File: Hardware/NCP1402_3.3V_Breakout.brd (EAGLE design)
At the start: 12.7 x 16.5 mm, 12 parts, among them U1 NCP1402

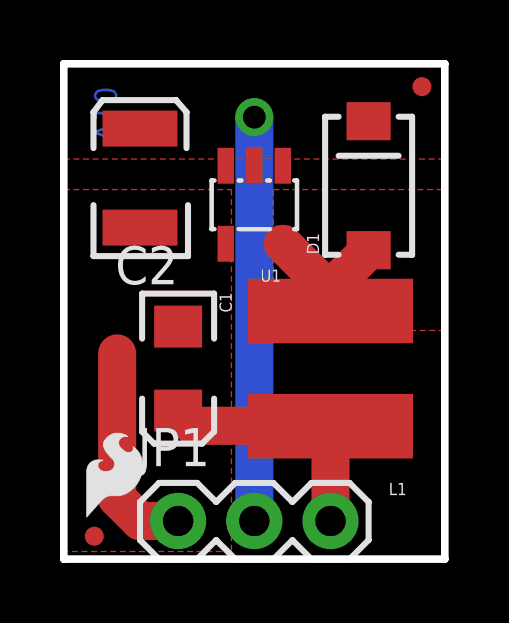
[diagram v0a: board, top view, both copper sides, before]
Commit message: changed micro fids to regular
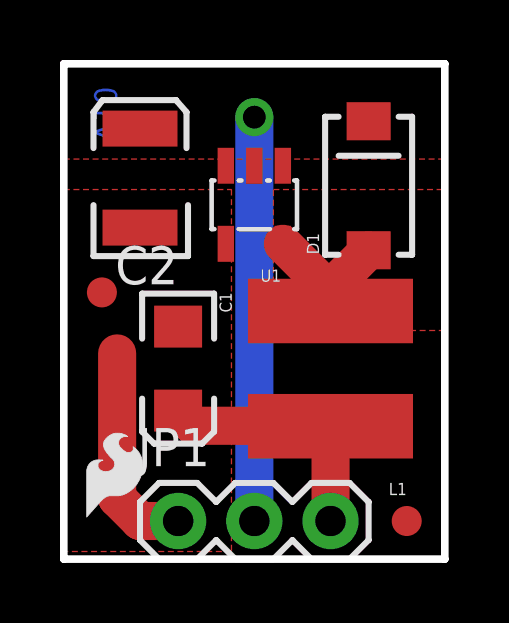
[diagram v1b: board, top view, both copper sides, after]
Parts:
- removed JP3, JP4: FIDUCIALUFIDUCIAL, SparkFun:MICRO-FIDUCIAL
- added FID1, FID2: FIDUCIAL1X2, SparkFun-Aesthetics:FIDUCIAL-1X2
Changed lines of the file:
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@@
 <?xml version="1.0" encoding="utf-8"?>
 <!DOCTYPE eagle SYSTEM "eagle.dtd">
-<eagle version="6.4">
+<eagle version="6.5.0">
 <drawing>
 <settings>
@@
 <setting verticaltext="up"/>
 </settings>
-<grid distance="0.05" unitdist="inch" unit="inch" style="lines" multiple="1" display="yes" altdistance="0.005" altunitdist="inch" altunit="inch"/>
+<grid distance="0.05" unitdist="inch" unit="inch" style="lines" multiple="1" display="yes" altdistance="0.01" altunitdist="inch" altunit="inch"/>
 <layers>
 <layer number="1" name="Top" color="4" fill="1" visible="yes" active="yes"/>
@@
 <layer number="18" name="Vias" color="2" fill="1" visible="yes" active="yes"/>
 <layer number="19" name="Unrouted" color="6" fill="1" visible="yes" active="yes"/>
-<layer number="20" name="Dimension" color="15" fill="1" visible="yes" active="yes"/>
-<layer number="21" name="tPlace" color="16" fill="1" visible="yes" active="yes"/>
-<layer number="22" name="bPlace" color="14" fill="1" visible="yes" active="yes"/>
+<layer number="20" name="Dimension" color="6" fill="1" visible="yes" active="yes"/>
+<layer number="21" name="tPlace" color="6" fill="1" visible="yes" active="yes"/>
+<layer number="22" name="bPlace" color="6" fill="1" visible="yes" active="yes"/>
 <layer number="23" name="tOrigins" color="15" fill="1" visible="yes" active="yes"/>
 <layer number="24" name="bOrigins" color="15" fill="1" visible="yes" active="yes"/>
@@
 <element name="JP2" library="SparkFun" package="SFE-LOGO-FLAME" value="LOGO-SFESK" x="0.762" y="1.397"/>
 <element name="U$1" library="SparkFun" package="OSHW-LOGO-S" value="OSHW-LOGOS" x="10.16" y="13.97" rot="MR90"/>
-<element name="JP3" library="SparkFun" package="MICRO-FIDUCIAL" value="FIDUCIALUFIDUCIAL" x="1.016" y="0.762"/>
-<element name="JP4" library="SparkFun" package="MICRO-FIDUCIAL" value="FIDUCIALUFIDUCIAL" x="11.938" y="15.748"/>
 <element name="U$2" library="SparkFun" package="CREATIVE_COMMONS" value="CREATIVE_COMMONS" x="-12.7" y="-17.78"/>
 <element name="FRAME1" library="SparkFun-Aesthetics" package="CREATIVE_COMMONS" value="FRAME-LETTER" x="-98.279478125" y="0"/>
+<element name="FID1" library="SparkFun-Aesthetics" package="FIDUCIAL-1X2" value="FIDUCIAL1X2" x="11.43" y="1.27"/>
+<element name="FID2" library="SparkFun-Aesthetics" package="FIDUCIAL-1X2" value="FIDUCIAL1X2" x="1.27" y="8.89"/>
 </elements>
 <signals>
